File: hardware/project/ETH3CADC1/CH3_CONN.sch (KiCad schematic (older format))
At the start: 1 part, among them J1201 Conn_02x10_Odd_Even

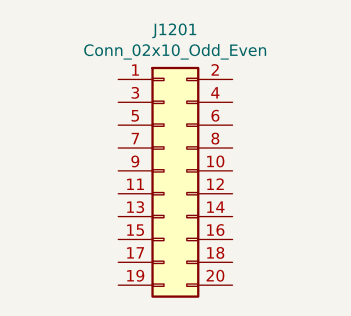
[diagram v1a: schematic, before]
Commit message: SDRAM works, thanks to the website https://medium.com/@pjinwoo123/stm32h7-external-sdram-evaluation-board-cc72444898d8 . Modified the code to work with SDRAM BANK2. SCPI library works.
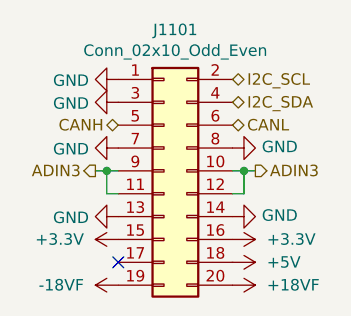
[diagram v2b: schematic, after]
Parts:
- renumbered J1201 to J1101
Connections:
- net GND: now reaches J1101.1 (Pin_1)
- net GND: now also J1101.13 (Pin_13), J1101.14 (Pin_14), J1101.3 (Pin_3), J1101.7 (Pin_7), J1101.8 (Pin_8)
- net ADIN3: now reaches J1101.10 (Pin_10)
- net ADIN3: now also J1101.11 (Pin_11), J1101.12 (Pin_12), J1101.9 (Pin_9)
- net +3V3: now reaches J1101.15 (Pin_15)
- net +3V3: now also J1101.16 (Pin_16)
- net +5V: now reaches J1101.18 (Pin_18)
- net -18VF: now reaches J1101.19 (Pin_19)
- net I2C_SCL: now reaches J1101.2 (Pin_2)
- net +18VF: now reaches J1101.20 (Pin_20)
- net I2C_SDA: now reaches J1101.4 (Pin_4)
- net CANH: now reaches J1101.5 (Pin_5)
- net CANL: now reaches J1101.6 (Pin_6)
- no-connect marks 0 -> 1
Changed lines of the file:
@@
 $Descr A4 11693 8268
 encoding utf-8
-Sheet 12 15
+Sheet 11 13
 Title ""
 Date ""
@@
 P 5700 3600
 AR Path="/60C206FB/60C2783C" Ref="J?"  Part="1"
-AR Path="/60C27246/60C2783C" Ref="J1201"  Part="1"
-F 0 "J1201" H 5750 4217 50  0000 C CNN
+AR Path="/60C27246/60C2783C" Ref="J1101"  Part="1"
+F 0 "J1101" H 5750 4217 50  0000 C CNN
 F 1 "Conn_02x10_Odd_Even" H 5750 4126 50  0000 C CNN
 F 2 "Connector_PinSocket_2.54mm:PinSocket_2x10_P2.54mm_Vertical" H 5700 3600 50  0001 C CNN
@@
 	1    0    0    -1
 $EndComp
+$Comp
+L power:GND #PWR?
+U 1 1 60626C67
+P 5500 3200
+AR Path="/60C206FB/60626C67" Ref="#PWR?"  Part="1"
+AR Path="/60C27246/60626C67" Ref="#PWR01101"  Part="1"
+F 0 "#PWR01101" H 5500 2950 50  0001 C CNN
+F 1 "GND" V 5505 3072 50  0000 R CNN
+F 2 "" H 5500 3200 50  0001 C CNN
+F 3 "" H 5500 3200 50  0001 C CNN
+	1    5500 3200
+	0    1    1    0
+$EndComp
+$Comp
+L power:GND #PWR?
+U 1 1 60626C6D
+P 5500 3300
+AR Path="/60C206FB/60626C6D" Ref="#PWR?"  Part="1"
+AR Path="/60C27246/60626C6D" Ref="#PWR01102"  Part="1"
+F 0 "#PWR01102" H 5500 3050 50  0001 C CNN
+F 1 "GND" V 5505 3172 50  0000 R CNN
+F 2 "" H 5500 3300 50  0001 C CNN
+F 3 "" H 5500 3300 50  0001 C CNN
+	1    5500 3300
+	0    1    1    0
+$EndComp
+$Comp
+L power:GND #PWR?
+U 1 1 60626C73
+P 5500 3500
+AR Path="/60C206FB/60626C73" Ref="#PWR?"  Part="1"
+AR Path="/60C27246/60626C73" Ref="#PWR01103"  Part="1"
+F 0 "#PWR01103" H 5500 3250 50  0001 C CNN
+F 1 "GND" V 5505 3372 50  0000 R CNN
+F 2 "" H 5500 3500 50  0001 C CNN
+F 3 "" H 5500 3500 50  0001 C CNN
+	1    5500 3500
+	0    1    1    0
+$EndComp
+$Comp
+L power:GND #PWR?
+U 1 1 60626C79
+P 6000 3500
+AR Path="/60C206FB/60626C79" Ref="#PWR?"  Part="1"
+AR Path="/60C27246/60626C79" Ref="#PWR01107"  Part="1"
+F 0 "#PWR01107" H 6000 3250 50  0001 C CNN
+F 1 "GND" V 6005 3372 50  0000 R CNN
+F 2 "" H 6000 3500 50  0001 C CNN
+F 3 "" H 6000 3500 50  0001 C CNN
+	1    6000 3500
+	0    -1   -1   0
+$EndComp
+$Comp
+L power:GND #PWR?
+U 1 1 60626C7F
+P 5500 3800
+AR Path="/60C206FB/60626C7F" Ref="#PWR?"  Part="1"
+AR Path="/60C27246/60626C7F" Ref="#PWR01104"  Part="1"
+F 0 "#PWR01104" H 5500 3550 50  0001 C CNN
+F 1 "GND" V 5505 3672 50  0000 R CNN
+F 2 "" H 5500 3800 50  0001 C CNN
+F 3 "" H 5500 3800 50  0001 C CNN
+	1    5500 3800
+	0    1    1    0
+$EndComp
+$Comp
+L power:GND #PWR?
+U 1 1 60626C85
+P 6000 3800
+AR Path="/60C206FB/60626C85" Ref="#PWR?"  Part="1"
+AR Path="/60C27246/60626C85" Ref="#PWR01108"  Part="1"
+F 0 "#PWR01108" H 6000 3550 50  0001 C CNN
+F 1 "GND" V 6005 3672 50  0000 R CNN
+F 2 "" H 6000 3800 50  0001 C CNN
+F 3 "" H 6000 3800 50  0001 C CNN
+	1    6000 3800
+	0    -1   -1   0
+$EndComp
+$Comp
+L power:+3.3V #PWR?
+U 1 1 60626C8B
+P 5500 3900
+AR Path="/60C206FB/60626C8B" Ref="#PWR?"  Part="1"
+AR Path="/60C27246/60626C8B" Ref="#PWR01105"  Part="1"
+F 0 "#PWR01105" H 5500 3750 50  0001 C CNN
+F 1 "+3.3V" V 5500 4050 50  0000 L CNN
+F 2 "" H 5500 3900 50  0001 C CNN
+F 3 "" H 5500 3900 50  0001 C CNN
+	1    5500 3900
+	0    -1   -1   0
+$EndComp
+$Comp
+L power:+3.3V #PWR?
+U 1 1 60626C91
+P 6000 3900
+AR Path="/60C206FB/60626C91" Ref="#PWR?"  Part="1"
+AR Path="/60C27246/60626C91" Ref="#PWR01109"  Part="1"
+F 0 "#PWR01109" H 6000 3750 50  0001 C CNN
+F 1 "+3.3V" V 6000 4050 50  0000 L CNN
+F 2 "" H 6000 3900 50  0001 C CNN
+F 3 "" H 6000 3900 50  0001 C CNN
+	1    6000 3900
+	0    1    1    0
+$EndComp
+NoConn ~ 5500 4000
+$Comp
+L power:+5V #PWR?
+U 1 1 60626C98
+P 6000 4000
+AR Path="/60C206FB/60626C98" Ref="#PWR?"  Part="1"
+AR Path="/60C27246/60626C98" Ref="#PWR01110"  Part="1"
+F 0 "#PWR01110" H 6000 3850 50  0001 C CNN
+F 1 "+5V" V 6000 4150 50  0000 L CNN
+F 2 "" H 6000 4000 50  0001 C CNN
+F 3 "" H 6000 4000 50  0001 C CNN
+	1    6000 4000
+	0    1    1    0
+$EndComp
+Wire Wire Line
+	6000 3600 6050 3600
+Wire Wire Line
+	6050 3600 6050 3700
+Wire Wire Line
+	6050 3700 6000 3700
+Wire Wire Line
+	5500 3700 5450 3700
+Wire Wire Line
+	5450 3700 5450 3600
+Wire Wire Line
+	5450 3600 5500 3600
+Text HLabel 6100 3600 2    50   Output ~ 0
+ADIN3
+Wire Wire Line
+	6100 3600 6050 3600
+Connection ~ 6050 3600
+Text HLabel 5400 3600 0    50   Output ~ 0
+ADIN3
+Wire Wire Line
+	5400 3600 5450 3600
+Connection ~ 5450 3600
+$Comp
+L ETH3CDAQ1:+18VF #PWR?
+U 1 1 60626CAA
+P 6000 4100
+AR Path="/60C206FB/60626CAA" Ref="#PWR?"  Part="1"
+AR Path="/60C27246/60626CAA" Ref="#PWR01111"  Part="1"
+F 0 "#PWR01111" H 6000 3950 50  0001 C CNN
+F 1 "+18VF" V 6000 4250 50  0000 L CNN
+F 2 "" H 6000 4100 50  0001 C CNN
+F 3 "" H 6000 4100 50  0001 C CNN
+	1    6000 4100
+	0    1    1    0
+$EndComp
+$Comp
+L ETH3CDAQ1:-18VF #PWR?
+U 1 1 60626CB0
+P 5500 4100
+AR Path="/60C206FB/60626CB0" Ref="#PWR?"  Part="1"
+AR Path="/60C27246/60626CB0" Ref="#PWR01106"  Part="1"
+F 0 "#PWR01106" H 5500 3950 50  0001 C CNN
+F 1 "-18VF" V 5500 4250 50  0000 L CNN
+F 2 "" H 5500 4100 50  0001 C CNN
+F 3 "" H 5500 4100 50  0001 C CNN
+	1    5500 4100
+	0    -1   -1   0
+$EndComp
+Text HLabel 5500 3400 0    50   BiDi ~ 0
+CANH
+Text HLabel 6000 3400 2    50   BiDi ~ 0
+CANL
+Text HLabel 6000 3200 2    50   BiDi ~ 0
+I2C_SCL
+Text HLabel 6000 3300 2    50   BiDi ~ 0
+I2C_SDA
 $EndSCHEMATC
